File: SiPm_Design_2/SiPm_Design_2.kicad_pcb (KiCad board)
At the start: 2 copper layers, 125.8 x 12.5 mm, 20 parts, among them IC1 OPA354AIDBVTG4, IC2 AFBR-S4N44P014M, IC3 AFBR-S4N44P014M, IC4 AFBR-S4N44P014M, IC5 AFBR-S4N44P014M, J3 1-1734839-0

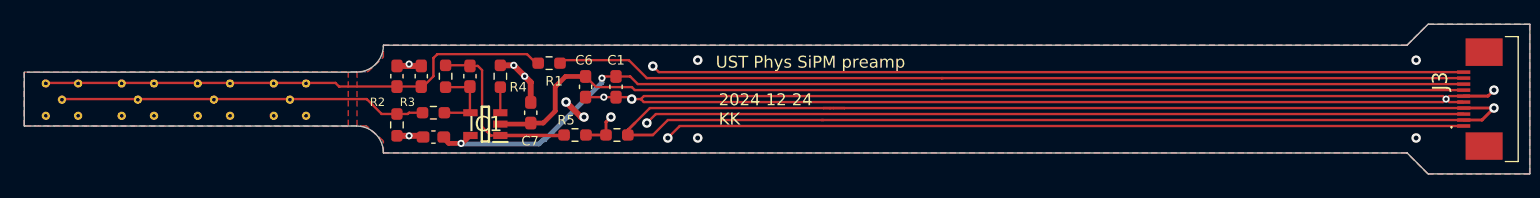
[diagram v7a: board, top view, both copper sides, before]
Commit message: fix soldermask on SiPM, change silkscreen
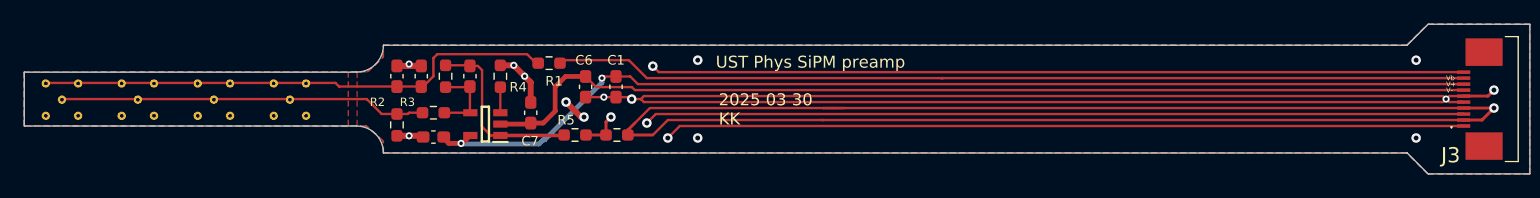
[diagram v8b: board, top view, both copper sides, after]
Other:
- outline, holes or cut-outs redrawn
- board text added: "2025 03 30 KK"
- board text added: "V+"
- board text added: "V-"
- board text added: "Vb"
- board text removed: "2024 12 24 KK"
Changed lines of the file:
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@@
 			(at 0 0 180)
 			(layer "F.SilkS")
+			(hide yes)
 			(effects
 				(font
@@
 		(tags "Connector")
 		(property "Reference" "J3"
-			(at 1.5 -4.25 90)
+			(at -4.699 -3.365 180)
 			(layer "F.SilkS")
 			(effects
@@
 		)
 		(pad "A1" thru_hole circle
-			(at 1.35 -1.35 90)
+			(at 1.35 -1.35 270)
 			(size 0.7 0.7)
 			(drill 0.3)
-			(layers "*.Cu" "B.Paste" "B.Mask")
+			(layers "*.Cu" "*.Mask" "B.Paste")
 			(remove_unused_layers no)
 			(net 2 "/Bias")
@@
 		)
 		(pad "A3" thru_hole circle
-			(at 1.35 1.35 90)
+			(at 1.35 1.35 270)
 			(size 0.7 0.7)
 			(drill 0.3)
-			(layers "*.Cu" "B.Paste" "B.Mask")
+			(layers "*.Cu" "*.Mask" "B.Paste")
 			(remove_unused_layers no)
 			(net 2 "/Bias")
@@
 		)
 		(pad "B2" thru_hole circle
-			(at 0 0 90)
+			(at 0 0 270)
 			(size 0.7 0.7)
 			(drill 0.3)
-			(layers "*.Cu" "B.Paste" "B.Mask")
+			(layers "*.Cu" "*.Mask" "B.Paste")
 			(remove_unused_layers no)
 			(net 4 "/anode")
@@
 		)
 		(pad "C1" thru_hole circle
-			(at -1.35 -1.35 90)
+			(at -1.35 -1.35 270)
 			(size 0.7 0.7)
 			(drill 0.3)
-			(layers "*.Cu" "B.Paste" "B.Mask")
+			(layers "*.Cu" "*.Mask" "B.Paste")
 			(remove_unused_layers no)
 			(net 2 "/Bias")
@@
 		)
 		(pad "C3" thru_hole circle
-			(at -1.35 1.35 90)
+			(at -1.35 1.35 270)
 			(size 0.7 0.7)
 			(drill 0.3)
-			(layers "*.Cu" "B.Paste" "B.Mask")
+			(layers "*.Cu" "*.Mask" "B.Paste")
 			(remove_unused_layers no)
 			(net 2 "/Bias")
@@
 		)
 		(pad "A1" thru_hole circle
-			(at 1.35 -1.35 90)
+			(at 1.35 -1.35 270)
 			(size 0.7 0.7)
 			(drill 0.3)
-			(layers "*.Cu" "B.Paste" "B.Mask")
+			(layers "*.Cu" "*.Mask" "B.Paste")
 			(remove_unused_layers no)
 			(net 2 "/Bias")
@@
 		)
 		(pad "A3" thru_hole circle
-			(at 1.35 1.35 90)
+			(at 1.35 1.35 270)
 			(size 0.7 0.7)
 			(drill 0.3)
-			(layers "*.Cu" "B.Paste" "B.Mask")
+			(layers "*.Cu" "*.Mask" "B.Paste")
 			(remove_unused_layers no)
 			(net 2 "/Bias")
@@
 		)
 		(pad "B2" thru_hole circle
-			(at 0 0 90)
+			(at 0 0 270)
 			(size 0.7 0.7)
 			(drill 0.3)
-			(layers "*.Cu" "B.Paste" "B.Mask")
+			(layers "*.Cu" "*.Mask" "B.Paste")
 			(remove_unused_layers no)
 			(net 4 "/anode")
@@
 		)
 		(pad "C1" thru_hole circle
-			(at -1.35 -1.35 90)
+			(at -1.35 -1.35 270)
 			(size 0.7 0.7)
 			(drill 0.3)
-			(layers "*.Cu" "B.Paste" "B.Mask")
+			(layers "*.Cu" "*.Mask" "B.Paste")
 			(remove_unused_layers no)
 			(net 2 "/Bias")
@@
 		)
 		(pad "C3" thru_hole circle
-			(at -1.35 1.35 90)
+			(at -1.35 1.35 270)
 			(size 0.7 0.7)
 			(drill 0.3)
-			(layers "*.Cu" "B.Paste" "B.Mask")
+			(layers "*.Cu" "*.Mask" "B.Paste")
 			(remove_unused_layers no)
 			(net 2 "/Bias")
@@
 		)
 		(pad "A1" thru_hole circle
-			(at 1.35 -1.35 90)
+			(at 1.35 -1.35 270)
 			(size 0.7 0.7)
 			(drill 0.3)
-			(layers "*.Cu" "B.Paste" "B.Mask")
+			(layers "*.Cu" "*.Mask" "B.Paste")
 			(remove_unused_layers no)
 			(net 2 "/Bias")
@@
 		)
 		(pad "A3" thru_hole circle
-			(at 1.35 1.35 90)
+			(at 1.35 1.35 270)
 			(size 0.7 0.7)
 			(drill 0.3)
-			(layers "*.Cu" "B.Paste" "B.Mask")
+			(layers "*.Cu" "*.Mask" "B.Paste")
 			(remove_unused_layers no)
 			(net 2 "/Bias")
@@
 		)
 		(pad "B2" thru_hole circle
-			(at 0 0 90)
+			(at 0 0 270)
 			(size 0.7 0.7)
 			(drill 0.3)
-			(layers "*.Cu" "B.Paste" "B.Mask")
+			(layers "*.Cu" "*.Mask" "B.Paste")
 			(remove_unused_layers no)
 			(net 4 "/anode")
@@
 		)
 		(pad "C1" thru_hole circle
-			(at -1.35 -1.35 90)
+			(at -1.35 -1.35 270)
 			(size 0.7 0.7)
 			(drill 0.3)
-			(layers "*.Cu" "B.Paste" "B.Mask")
+			(layers "*.Cu" "*.Mask" "B.Paste")
 			(remove_unused_layers no)
 			(net 2 "/Bias")
@@
 		)
 		(pad "C3" thru_hole circle
-			(at -1.35 1.35 90)
+			(at -1.35 1.35 270)
 			(size 0.7 0.7)
 			(drill 0.3)
-			(layers "*.Cu" "B.Paste" "B.Mask")
+			(layers "*.Cu" "*.Mask" "B.Paste")
 			(remove_unused_layers no)
 			(net 2 "/Bias")
@@
 		)
 		(pad "A1" thru_hole circle
-			(at 1.35 -1.35 90)
+			(at 1.35 -1.35 270)
 			(size 0.7 0.7)
 			(drill 0.3)
-			(layers "*.Cu" "B.Paste" "B.Mask")
+			(layers "*.Cu" "*.Mask" "B.Paste")
 			(remove_unused_layers no)
 			(net 2 "/Bias")
@@
 		)
 		(pad "A3" thru_hole circle
-			(at 1.35 1.35 90)
+			(at 1.35 1.35 270)
 			(size 0.7 0.7)
 			(drill 0.3)
-			(layers "*.Cu" "B.Paste" "B.Mask")
+			(layers "*.Cu" "*.Mask" "B.Paste")
 			(remove_unused_layers no)
 			(net 2 "/Bias")
@@
 		)
 		(pad "B2" thru_hole circle
-			(at 0 0 90)
+			(at 0 0 270)
 			(size 0.7 0.7)
 			(drill 0.3)
-			(layers "*.Cu" "B.Paste" "B.Mask")
+			(layers "*.Cu" "*.Mask" "B.Paste")
 			(remove_unused_layers no)
 			(net 4 "/anode")
@@
 		)
 		(pad "C1" thru_hole circle
-			(at -1.35 -1.35 90)
+			(at -1.35 -1.35 270)
 			(size 0.7 0.7)
 			(drill 0.3)
-			(layers "*.Cu" "B.Paste" "B.Mask")
+			(layers "*.Cu" "*.Mask" "B.Paste")
 			(remove_unused_layers no)
 			(net 2 "/Bias")
@@
 		)
 		(pad "C3" thru_hole circle
-			(at -1.35 1.35 90)
+			(at -1.35 1.35 270)
 			(size 0.7 0.7)
 			(drill 0.3)
-			(layers "*.Cu" "B.Paste" "B.Mask")
+			(layers "*.Cu" "*.Mask" "B.Paste")
 			(remove_unused_layers no)
 			(net 2 "/Bias")
@@
 	)
 	(gr_line
-		(start 129.388 105.454)
+		(start 129.138 105.454)
 		(end 156.888 105.454)
 		(stroke
@@
 		(layer "User.2")
 	)
+	(gr_text "Vb"
+		(at 247.892 106.18 0)
+		(layer "F.SilkS")
+		(effects
+			(font
+				(size 0.4 0.4)
+				(thickness 0.1)
+			)
+			(justify left bottom)
+		)
+	)
+	(gr_text "V+"
+		(at 247.892 106.688 0)
+		(layer "F.SilkS")
+		(effects
+			(font
+				(size 0.4 0.4)
+				(thickness 0.1)
+			)
+			(justify left bottom)
+		)
+	)
 	(gr_text "UST Phys SiPM preamp"
 		(at 186.888 105.204 0)
@@
 		)
 	)
-	(gr_text "2024 12 24 \nKK"
+	(gr_text "V-"
+		(at 247.892 107.196 0)
+		(layer "F.SilkS")
+		(effects
+			(font
+				(size 0.4 0.4)
+				(thickness 0.1)
+			)
+			(justify left bottom)
+		)
+	)
+	(gr_text "2025 03 30 \nKK"
 		(at 187.138 109.954 0)
 		(layer "F.SilkS")
@@
 			(clearance 0.25)
 		)
-		(min_thickness 0.25)
+		(min_thickness 0.2)
 		(filled_areas_thickness no)
 		(fill yes
